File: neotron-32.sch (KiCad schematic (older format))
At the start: 3 parts, among them J101 Conn_02x06, J102 Conn_02x06, U101 TM4C123G_Launchpad

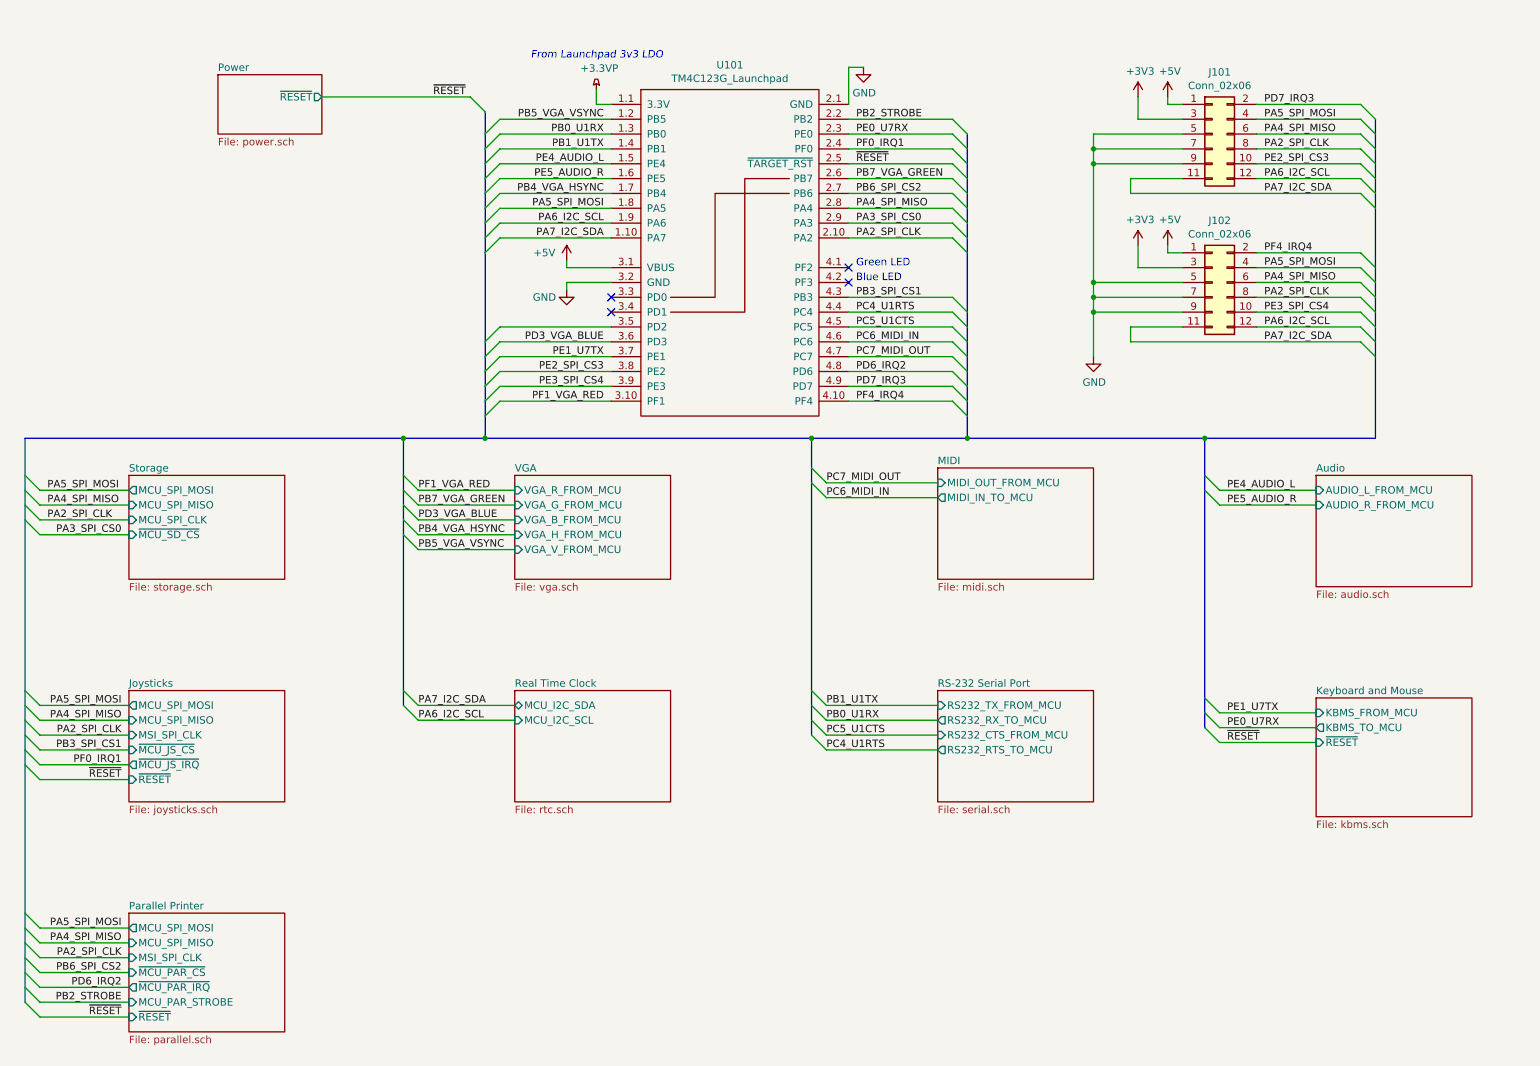
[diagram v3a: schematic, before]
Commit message: Schematic capture draft complete.
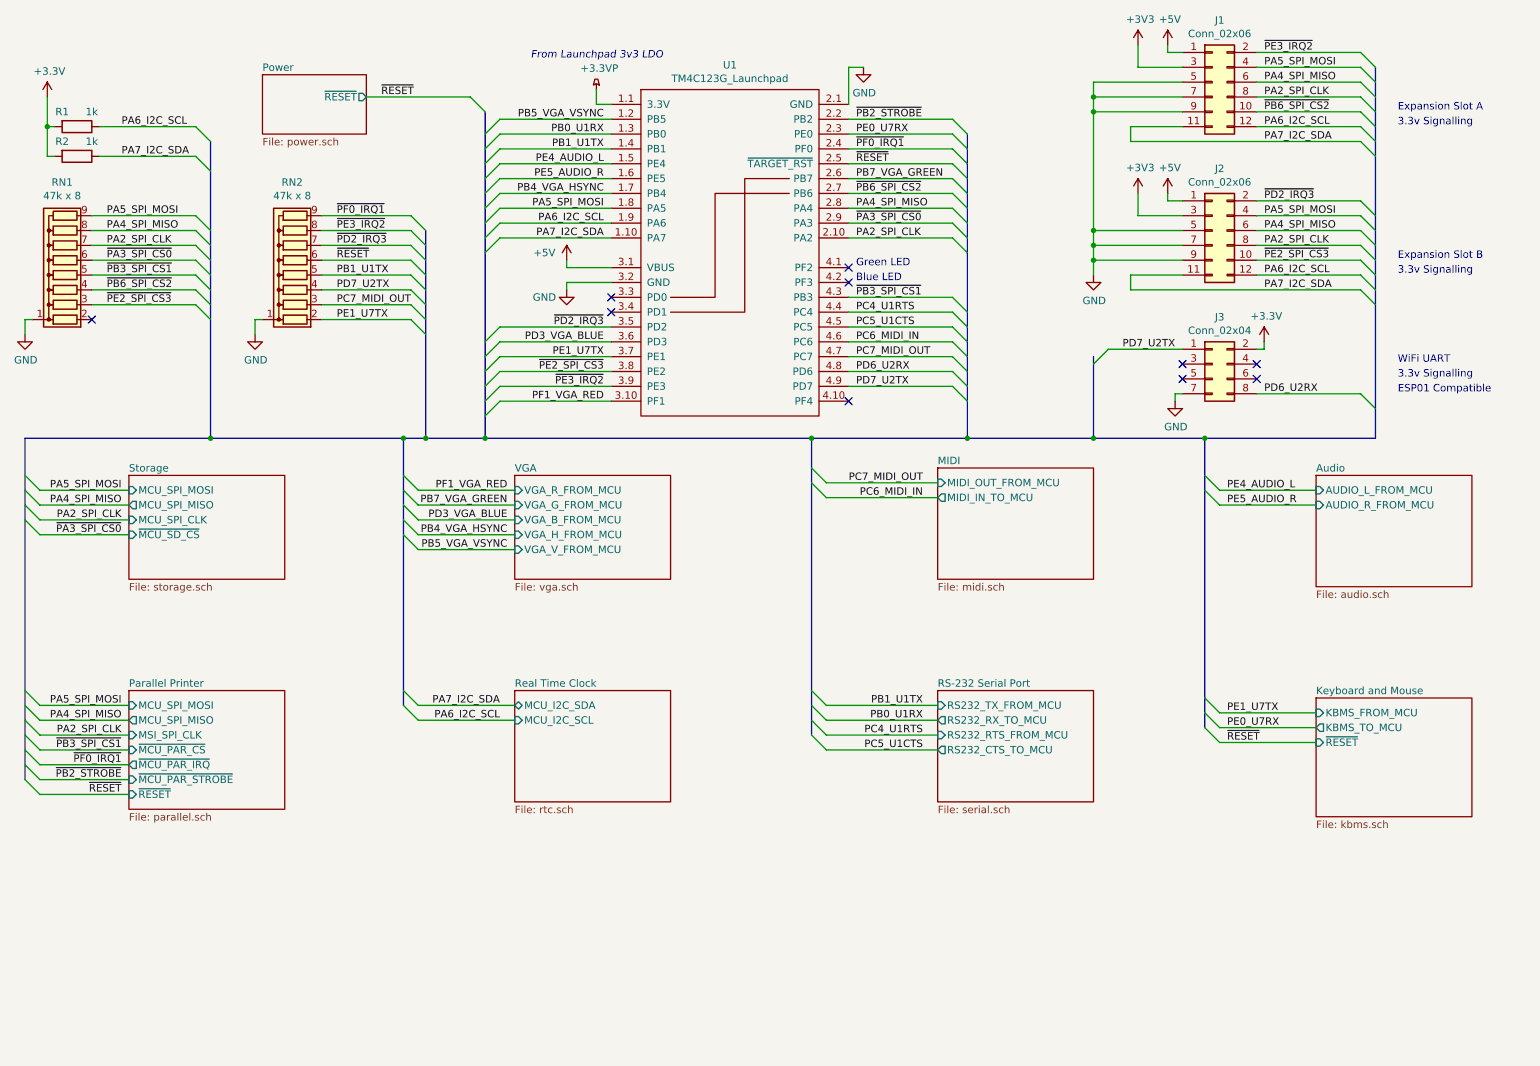
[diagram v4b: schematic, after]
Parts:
- added J3: Conn_02x04, symbol Connector_Generic:Conn_02x04_Odd_Even
- added R1, R2: 1k, Resistor_THT:R_Axial_DIN0411_L9.9mm_D3.6mm_P12.70mm_Horizontal, symbol Device:R
- added RN1, RN2: 47k x 8, Resistor_THT:R_Array_SIP9, symbol Device:R_Network08
- renumbered J101 to J1, J102 to J2, U101 to U1
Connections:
- net +3V3: now also J3.2 (Pin_2), R1.2, R2.2
- net GND: now also J3.7 (Pin_7), RN1.1 (common), RN2.1 (common)
- net PA2_SPI_CLK: now also RN1.7 (R6)
- net PA4_SPI_MISO: now also RN1.8 (R7)
- net PA5_SPI_MOSI: now also RN1.9 (R8)
- net PA6_I2C_SCL: now also R1.1
- net PA7_I2C_SDA: now also R2.1
- net PB1_U1TX: now also RN2.5 (R4)
- net PC7_MIDI_OUT: now also RN2.3 (R2)
- net PE1_U7TX: now also RN2.2 (R1)
- net ~RESET: now also RN2.6 (R5)
- net ~PD2_IRQ3: now reaches U1.3.5 (PD2)
- net ~PD2_IRQ3: now also J2.2 (Pin_2), RN2.7 (R6)
- net PA3_SPI_CS0 renamed ~PA3_SPI_CS0
- net ~PA3_SPI_CS0: now also RN1.6 (R5)
- net PB2_STROBE renamed ~PB2_STROBE
- net PB3_SPI_CS1 renamed ~PB3_SPI_CS1
- net ~PB3_SPI_CS1: now also RN1.5 (R4)
- net PB6_SPI_CS2 renamed ~PB6_SPI_CS2
- net ~PB6_SPI_CS2: now also J1.10 (Pin_10), RN1.4 (R3)
- net PD6_IRQ2 renamed PD6_U2RX
- net PD6_U2RX: now also J3.8 (Pin_8)
- net PD7_IRQ3 renamed PD7_U2TX
- net PD7_U2TX: now also J3.1 (Pin_1), RN2.4 (R3); no longer J1.2 (Pin_2)
- net PE2_SPI_CS3 renamed ~PE2_SPI_CS3
- net ~PE2_SPI_CS3: now also J2.10 (Pin_10), RN1.3 (R2); no longer J1.10 (Pin_10)
- net PE3_SPI_CS4 renamed ~PE3_IRQ2
- net ~PE3_IRQ2: now also J1.2 (Pin_2), RN2.8 (R7); no longer J2.10 (Pin_10)
- net PF0_IRQ1 renamed ~PF0_IRQ1
- net ~PF0_IRQ1: now also RN2.9 (R8)
- net PF4_IRQ4: no longer names the net of U1.4.10 (PF4)
- net PF4_IRQ4: no longer J2.2 (Pin_2)
- no-connect marks 4 -> 10
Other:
- note added: "3.3v Signalling"
- note added: "ESP01 Compatible"
- note added: "Expansion Slot A"
- note added: "Expansion Slot B"
- note added: "WiFi UART"
- moved on the sheet: J1, J2

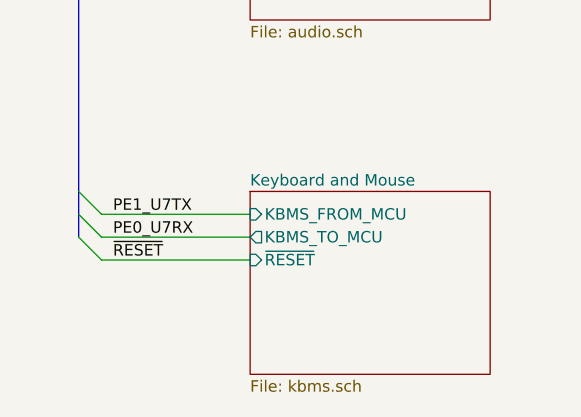
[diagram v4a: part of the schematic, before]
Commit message: Tidied up Atmega power. Added page titles.
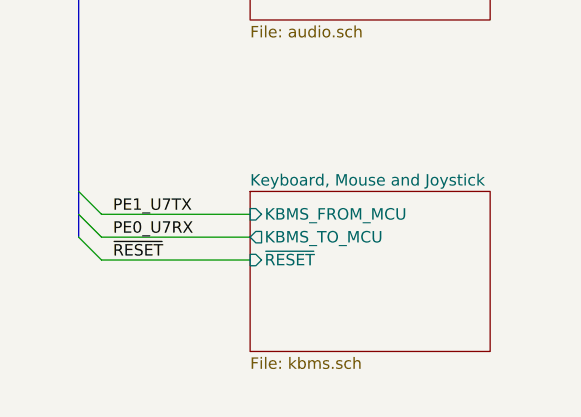
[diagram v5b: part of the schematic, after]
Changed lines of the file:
@@
 Sheet 1 10
 Title "Neotron 32K Main PCB"
-Date "2019-12-15"
-Rev "0.5"
+Date "2019-12-16"
+Rev "0.6"
 Comp "github.com/neotron-compute/Neotron-32-Hardware"
 Comment1 "Copyright (c) Jonathan 'theJPster' Pallant"
@@
 $EndSheet
 $Sheet
-S 9650 5200 1050 800
+S 9650 5200 1050 700
 U 5DF2662E
-F0 "Keyboard and Mouse" 50
+F0 "Keyboard, Mouse and Joystick" 50
 F1 "kbms.sch" 50
 F2 "KBMS_FROM_MCU" I L 9650 5300 50

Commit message: Work in progress.
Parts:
- added H1, H2, H3, H4: MountingHole, MountingHole:MountingHole_3.2mm_M3, symbol Mechanical:MountingHole
- J3: footprint (none) -> Connector_PinHeader_2.54mm:PinHeader_2x04_P2.54mm_Vertical
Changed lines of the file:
@@
 F 0 "J3" H 9000 3267 50  0000 C CNN
 F 1 "Conn_02x04" H 9000 3176 50  0000 C CNN
-F 2 "" H 8950 2950 50  0001 C CNN
+F 2 "Connector_PinHeader_2.54mm:PinHeader_2x04_P2.54mm_Vertical" H 8950 2950 50  0001 C CNN
 F 3 "~" H 8950 2950 50  0001 C CNN
 	1    8950 2950
@@
 Text Notes 10200 3150 0    50   ~ 0
 ESP01 Compatible
+$Comp
+L Mechanical:MountingHole H1
+U 1 1 5DFC719B
+P 1550 6900
+F 0 "H1" H 1650 6946 50  0000 L CNN
+F 1 "MountingHole" H 1650 6855 50  0000 L CNN
+F 2 "MountingHole:MountingHole_3.2mm_M3" H 1550 6900 50  0001 C CNN
+F 3 "~" H 1550 6900 50  0001 C CNN
+	1    1550 6900
+	1    0    0    -1
+$EndComp
+$Comp
+L Mechanical:MountingHole H2
+U 1 1 5DFC7744
+P 1550 7100
+F 0 "H2" H 1650 7146 50  0000 L CNN
+F 1 "MountingHole" H 1650 7055 50  0000 L CNN
+F 2 "MountingHole:MountingHole_3.2mm_M3" H 1550 7100 50  0001 C CNN
+F 3 "~" H 1550 7100 50  0001 C CNN
+	1    1550 7100
+	1    0    0    -1
+$EndComp
+$Comp
+L Mechanical:MountingHole H3
+U 1 1 5DFC781B
+P 1550 7300
+F 0 "H3" H 1650 7346 50  0000 L CNN
+F 1 "MountingHole" H 1650 7255 50  0000 L CNN
+F 2 "MountingHole:MountingHole_3.2mm_M3" H 1550 7300 50  0001 C CNN
+F 3 "~" H 1550 7300 50  0001 C CNN
+	1    1550 7300
+	1    0    0    -1
+$EndComp
+$Comp
+L Mechanical:MountingHole H4
+U 1 1 5DFC799C
+P 1550 7500
+F 0 "H4" H 1650 7546 50  0000 L CNN
+F 1 "MountingHole" H 1650 7455 50  0000 L CNN
+F 2 "MountingHole:MountingHole_3.2mm_M3" H 1550 7500 50  0001 C CNN
+F 3 "~" H 1550 7500 50  0001 C CNN
+	1    1550 7500
+	1    0    0    -1
+$EndComp
 Wire Bus Line
 	8150 2900 8150 3450

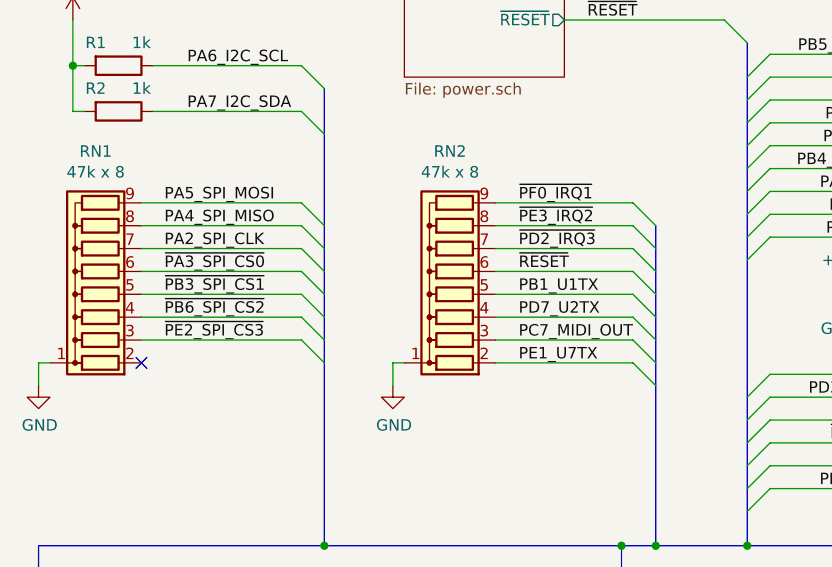
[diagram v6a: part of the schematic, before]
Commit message: Updated footprints: ) Swapped RS-232 DE9 for IDC header. ) Large caps are radial electrolytics. ) Made resistors a little smaller.
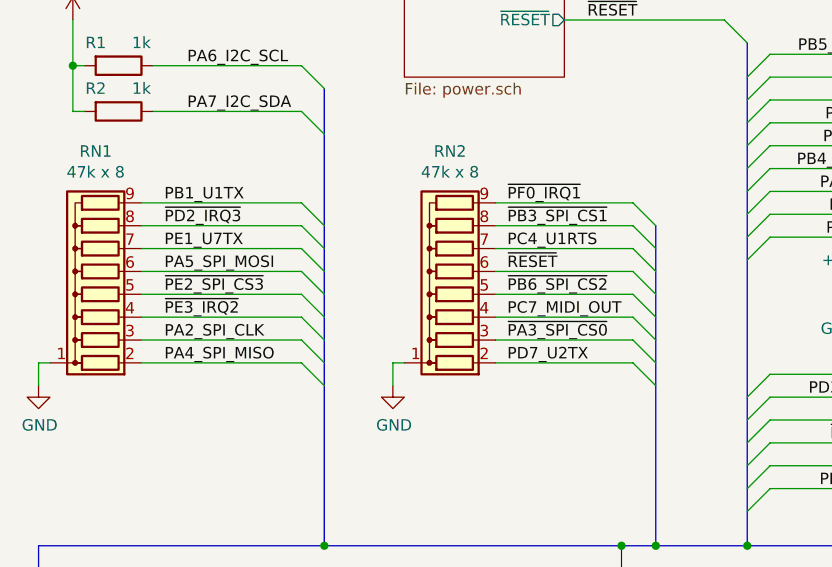
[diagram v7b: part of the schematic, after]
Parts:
- R1, R2: footprint Resistor_THT:R_Axial_DIN0411_L9.9mm_D3.6mm_P12.70mm_Horizontal -> Resistor_THT:R_Axial_DIN0207_L6.3mm_D2.5mm_P10.16mm_Horizontal
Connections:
- net PA2_SPI_CLK: now also RN1.3 (R2); no longer RN1.7 (R6)
- net PA4_SPI_MISO: now also RN1.2 (R1); no longer RN1.8 (R7)
- net PA5_SPI_MOSI: now also RN1.6 (R5); no longer RN1.9 (R8)
- net PB1_U1TX: now also RN1.9 (R8); no longer RN2.5 (R4)
- net PC4_U1RTS: now also RN2.7 (R6)
- net PC7_MIDI_OUT: now also RN2.4 (R3); no longer RN2.3 (R2)
- net PD7_U2TX: now also RN2.2 (R1); no longer RN2.4 (R3)
- net PE1_U7TX: now also RN1.7 (R6); no longer RN2.2 (R1)
- net ~PA3_SPI_CS0: now also RN2.3 (R2); no longer RN1.6 (R5)
- net ~PB3_SPI_CS1: now also RN2.8 (R7); no longer RN1.5 (R4)
- net ~PB6_SPI_CS2: now also RN2.5 (R4); no longer RN1.4 (R3)
- net ~PD2_IRQ3: now also RN1.8 (R7); no longer RN2.7 (R6)
- net ~PE2_SPI_CS3: now also RN1.5 (R4); no longer RN1.3 (R2)
- net ~PE3_IRQ2: now also RN1.4 (R3); no longer RN2.8 (R7)
- no-connect marks 10 -> 9
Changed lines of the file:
@@
 	0    -1   -1   0
 $EndComp
-Text Label 1500 1950 0    50   ~ 0
+Text Label 1500 2250 0    50   ~ 0
 PA5_SPI_MOSI
-Text Label 1500 2050 0    50   ~ 0
+Text Label 1500 2650 0    50   ~ 0
 PA4_SPI_MISO
-Text Label 1500 2150 0    50   ~ 0
-PA2_SPI_CLK
-Text Label 1500 2550 0    50   ~ 0
+Text Label 1500 2350 0    50   ~ 0
 ~PE2_SPI_CS3
-Text Label 3050 1950 0    50   ~ 0
+Text Label 3000 1950 0    50   ~ 0
 ~PF0_IRQ1
-Text Label 3050 2250 0    50   ~ 0
+Text Label 3000 2250 0    50   ~ 0
 ~RESET
-Text Label 1500 2350 0    50   ~ 0
+Text Label 3000 2050 0    50   ~ 0
 ~PB3_SPI_CS1
-Text Label 1500 2250 0    50   ~ 0
+Text Label 3000 2550 0    50   ~ 0
 ~PA3_SPI_CS0
-Text Label 1500 2450 0    50   ~ 0
+Text Label 3000 2350 0    50   ~ 0
 ~PB6_SPI_CS2
 $Comp
@@
 F 0 "R2" V 1200 1450 50  0000 C CNN
 F 1 "1k" V 1200 1650 50  0000 C CNN
-F 2 "Resistor_THT:R_Axial_DIN0411_L9.9mm_D3.6mm_P12.70mm_Horizontal" V 1230 1550 50  0001 C CNN
+F 2 "Resistor_THT:R_Axial_DIN0207_L6.3mm_D2.5mm_P10.16mm_Horizontal" V 1230 1550 50  0001 C CNN
 F 3 "~" H 1300 1550 50  0001 C CNN
 	1    1300 1550
@@
 F 0 "R1" V 1200 1250 50  0000 C CNN
 F 1 "1k" V 1200 1450 50  0000 C CNN
-F 2 "Resistor_THT:R_Axial_DIN0411_L9.9mm_D3.6mm_P12.70mm_Horizontal" V 1230 1350 50  0001 C CNN
+F 2 "Resistor_THT:R_Axial_DIN0207_L6.3mm_D2.5mm_P10.16mm_Horizontal" V 1230 1350 50  0001 C CNN
 F 3 "~" H 1300 1350 50  0001 C CNN
 	1    1300 1350
@@
 Wire Wire Line
 	3550 2450 2950 2450
-Text Label 3050 2550 0    50   ~ 0
+Text Label 3000 2450 0    50   ~ 0
 PC7_MIDI_OUT
-Text Label 3050 2350 0    50   ~ 0
+Text Label 1500 1950 0    50   ~ 0
 PB1_U1TX
-Text Label 3050 2650 0    50   ~ 0
+Text Label 1500 2150 0    50   ~ 0
 PE1_U7TX
-NoConn ~ 1400 2650
 Wire Wire Line
 	4900 2700 4150 2700
@@
 Wire Wire Line
 	9250 3150 9950 3150
-Text Label 3050 2050 0    50   ~ 0
+Text Label 1500 2450 0    50   ~ 0
 ~PE3_IRQ2
-Text Label 3050 2150 0    50   ~ 0
+Text Label 1500 2050 0    50   ~ 0
 ~PD2_IRQ3
-Text Label 3050 2450 0    50   ~ 0
+Text Label 3000 2650 0    50   ~ 0
 PD7_U2TX
 Text Notes 10200 1350 0    50   ~ 0
@@
 	1    0    0    -1
 $EndComp
+Text Label 1500 2550 0    50   ~ 0
+PA2_SPI_CLK
+Text Label 3000 2150 0    50   ~ 0
+PC4_U1RTS
+Wire Wire Line
+	1400 2650 2100 2650
 Wire Bus Line
 	8150 2900 8150 3450
@@
 Wire Bus Line
 	10050 950  10050 3450
+Entry Wire Line
+	2100 2650 2200 2750
 $EndSCHEMATC

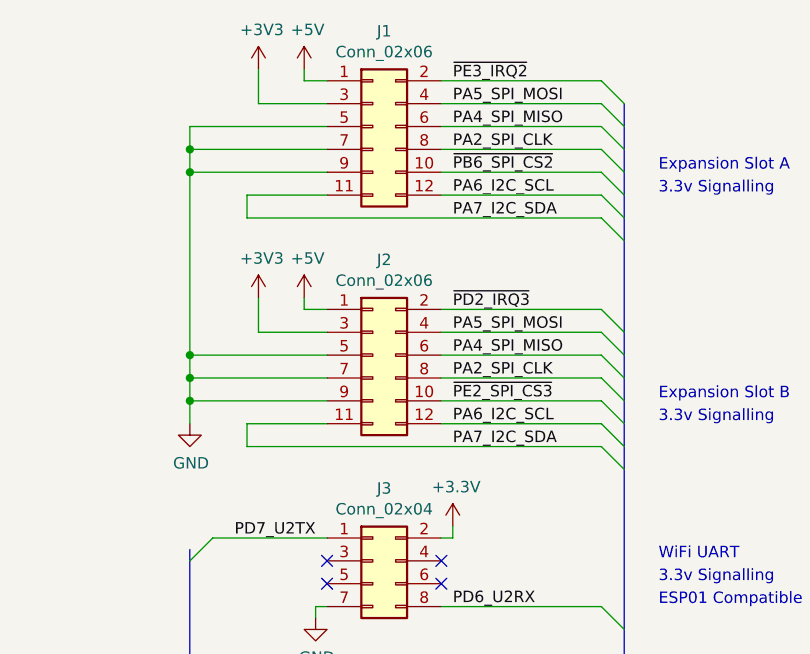
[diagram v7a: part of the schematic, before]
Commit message: First draft layout complete. Fixing DRC issues.
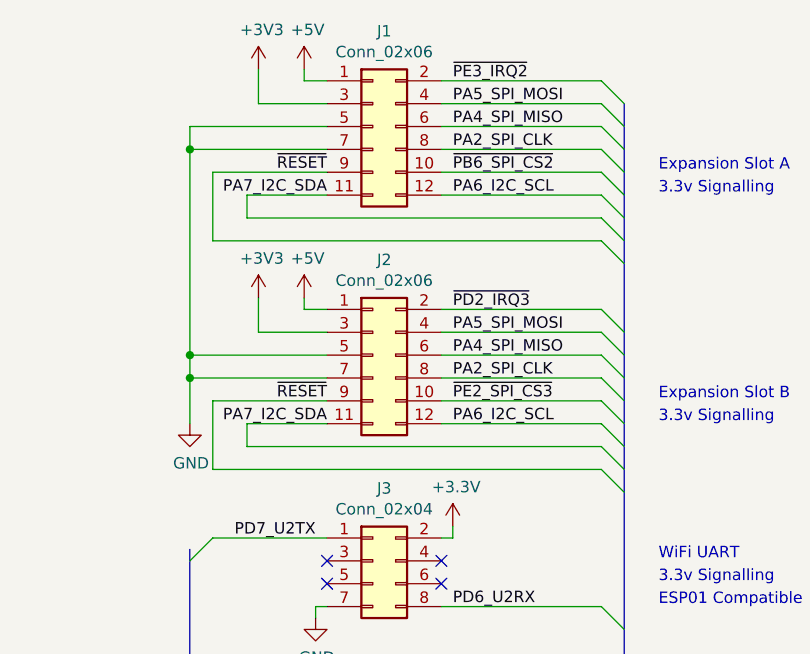
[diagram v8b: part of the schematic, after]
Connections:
- net GND: no longer J1.9 (Pin_9), J2.9 (Pin_9)
- net ~RESET: now also J1.9 (Pin_9), J2.9 (Pin_9)
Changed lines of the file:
@@
 Text Label 9300 1150 0    50   ~ 0
 PA2_SPI_CLK
-Text Label 9300 1450 0    50   ~ 0
+Text Label 8750 1350 2    50   ~ 0
 PA7_I2C_SDA
 Entry Wire Line
@@
 Text Label 9300 2350 0    50   ~ 0
 PA6_I2C_SCL
-Text Label 9300 2450 0    50   ~ 0
+Text Label 8750 2350 2    50   ~ 0
 PA7_I2C_SDA
 Entry Wire Line
@@
 $EndComp
 Wire Wire Line
-	8150 2250 8750 2250
-Wire Wire Line
 	8150 2050 8150 2150
 Wire Wire Line
@@
 Connection ~ 8150 2150
 Wire Wire Line
-	8150 2150 8150 2250
-Wire Wire Line
 	8150 1050 8150 1150
 Wire Wire Line
@@
 	8150 1150 8750 1150
 Connection ~ 8150 1150
-Wire Wire Line
-	8150 1150 8150 1250
-Wire Wire Line
-	8150 1250 8750 1250
-Connection ~ 8150 1250
-Wire Wire Line
-	8150 1250 8150 2050
 $Comp
 L power:+5V #PWR012
@@
 Entry Wire Line
 	8150 2950 8250 2850
-Wire Wire Line
-	8150 2250 8150 2350
-Connection ~ 8150 2250
 Wire Bus Line
 	7300 3450 8150 3450
@@
 Wire Wire Line
 	1400 2650 2100 2650
+Entry Wire Line
+	2100 2650 2200 2750
+Wire Wire Line
+	8150 1150 8150 2050
+Wire Wire Line
+	8150 2150 8150 2350
+Entry Wire Line
+	9950 1550 10050 1650
+Entry Wire Line
+	9950 2550 10050 2650
+Text Label 8750 2250 2    50   ~ 0
+~RESET
+Text Label 8750 1250 2    50   ~ 0
+~RESET
+Wire Wire Line
+	8250 2250 8250 2550
+Wire Wire Line
+	8250 2250 8750 2250
+Wire Wire Line
+	8250 2550 9950 2550
+Wire Wire Line
+	8250 1250 8250 1550
+Wire Wire Line
+	8250 1250 8750 1250
+Wire Wire Line
+	8250 1550 9950 1550
 Wire Bus Line
 	8150 2900 8150 3450
@@
 	3500 3450 3500 5250
 Wire Bus Line
+	2200 1450 2200 3450
+Wire Bus Line
 	3650 2050 3650 3450
 Wire Bus Line
-	2200 1450 2200 3450
-Wire Bus Line
 	950  3450 950  5750
 Wire Bus Line
@@
 Wire Bus Line
 	10050 950  10050 3450
-Entry Wire Line
-	2100 2650 2200 2750
 $EndSCHEMATC
